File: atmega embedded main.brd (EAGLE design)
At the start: 313.5 x 125.9 mm, 150 parts, among them IC1 ATMEGA328PROUND, K100 SWITCH, K101 SWITCH, K102 SWITCH, K103 SWITCH, K104 SWITCH, K105 SWITCH, K106 SWITCH, K107 SWITCH, K108 SWITCH, K109 SWITCH, K110 SWITCH, K111 SWITCH, K112 SWITCH, K113 SWITCH, K114 SWITCH, K115 SWITCH, K116 SWITCH, K117 SWITCH, K118 SWITCH, K119 SWITCH, K120 SWITCH, K121 SWITCH, K122 SWITCH, K123 SWITCH, K124 SWITCH, K125 SWITCH, K126 SWITCH, K127 SWITCH, K128 SWITCH, K129 SWITCH, K130 SWITCH, K60 SWITCH, K67 SWITCH, K68 SWITCH, K69 SWITCH, K70 SWITCH, K71 SWITCH, K72 SWITCH, K73 SWITCH, K74 SWITCH, K75 SWITCH, K76 SWITCH, K77 SWITCH, K78 SWITCH, K79 SWITCH, K80 SWITCH, K81 SWITCH, K82 SWITCH, K83 SWITCH, K84 SWITCH, K85 SWITCH, K86 SWITCH, K87 SWITCH, K88 SWITCH, K89 SWITCH, K90 SWITCH, K91 SWITCH, K92 SWITCH, K93 SWITCH, K94 SWITCH, K95 SWITCH, K96 SWITCH, K97 SWITCH, K98 SWITCH, K99 SWITCH

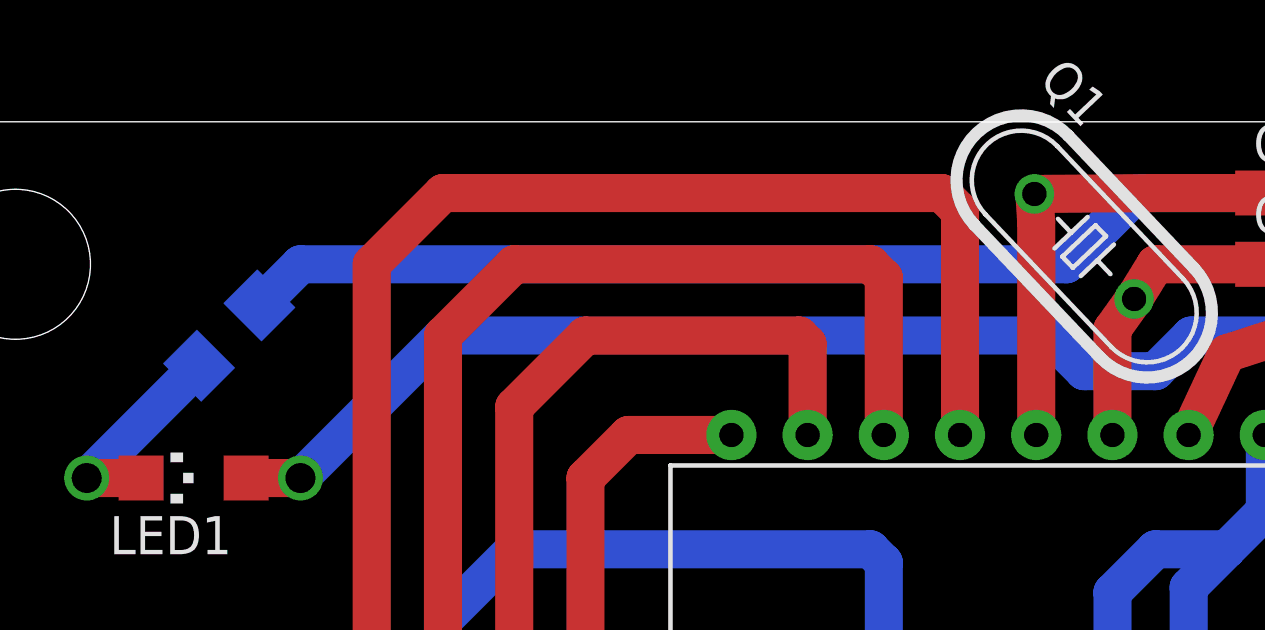
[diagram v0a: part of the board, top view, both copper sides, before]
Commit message: Finished Marko's board and fixed some errors.
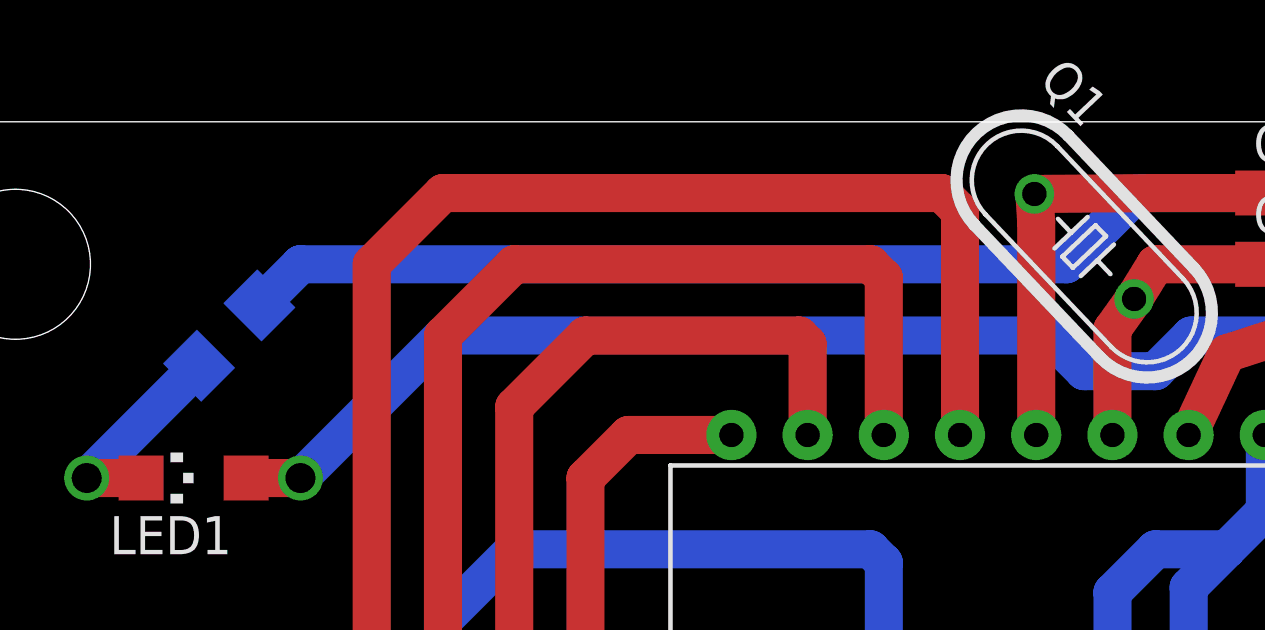
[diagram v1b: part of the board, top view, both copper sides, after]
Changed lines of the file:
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@@
 <wire x1="108.2594" y1="106.875" x2="83.125" y2="106.875" width="1.27" layer="16"/>
 <contactref element="R3" pad="2"/>
-<wire x1="3.380503125" y1="110.255503125" x2="4.75" y2="111.625" width="1.27" layer="16"/>
-<wire x1="4.75" y1="111.625" x2="30.28125" y2="111.625" width="1.27" layer="16"/>
+<wire x1="30.28125" y1="111.625" x2="4.75" y2="111.625" width="1.27" layer="16"/>
 <wire x1="30.28125" y1="111.625" x2="32.65625" y2="114" width="1.27" layer="16"/>
 <wire x1="32.65625" y1="114" x2="80.75" y2="114" width="1.27" layer="16"/>
@@
 <wire x1="120.7875" y1="106.875" x2="120.7875" y2="110.4375" width="1.27" layer="1"/>
 <wire x1="120.7875" y1="110.4375" x2="120.7875" y2="114" width="1.27" layer="1"/>
-<wire x1="3.380503125" y1="110.255503125" x2="3.38050625" y2="110.255503125" width="0" layer="19" extent="16-16"/>
+<wire x1="4.75" y1="111.625" x2="4.75" y2="111.624996875" width="1.27" layer="16"/>
+<wire x1="4.75" y1="111.624996875" x2="3.38050625" y2="110.255503125" width="1.27" layer="16"/>
 </signal>
 <signal name="VCC">
@@
 <via x="-2.375" y="104.5" extent="1-16" drill="1"/>
 <wire x1="-2.375" y1="104.5" x2="1.36949375" y2="108.24449375" width="1.27" layer="16"/>
-<wire x1="1.36949375" y1="108.24449375" x2="1.369496875" y2="108.24449375" width="0" layer="19" extent="16-16"/>
+<wire x1="1.36949375" y1="108.24449375" x2="1.369496875" y2="108.24449375" width="1.27" layer="16"/>
 </signal>
 </signals>

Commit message: Less Horrible for Marko no.1
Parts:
- moved D96 13.1 mm to (117.6, 42.0), turned to 0 degrees
- moved D73 12.8 mm to (117.6, 61.8), turned to 0 degrees
- moved D97 12.7 mm to (117.6, 24.0), turned to 0 degrees
- moved D72 12.5 mm to (117.6, 81.5), turned to 0 degrees
- moved D79 11.6 mm to (-5.25, 63.4), turned to 90 degrees
- moved D45 11.4 mm to (-5.00, 82.4), turned to 90 degrees
- moved D80 11.4 mm to (-5.00, 44.4), turned to 90 degrees
- moved D81 11.4 mm to (-5.00, 25.4), turned to 90 degrees
- moved D82 11.4 mm to (-5.00, 6.44), turned to 90 degrees
- moved LED1 7.21 mm to (5.19, 110.5)
- moved D63 4.72 mm to (22.4, 81.5)
- moved R3 4.61 mm to (1.38, 113.8)
- moved D78 4.26 mm to (22.3, 62.2)
- moved D98 4.26 mm to (164.8, 24.2)
- moved D115 4.01 mm to (288.3, 81.5)
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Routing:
- net ROW5: track 766.2 -> 354.9 mm, vias 2 -> 3
- net ROW3: track 646.0 -> 262.5 mm, vias 2 -> 3
- net ROW4: track 658.2 -> 460.7 mm, vias 2 -> 9
- net COL6: track 277.7 -> 445.6 mm, vias 2 -> 7
- net ROW2: track 600.6 -> 469.0 mm, vias 2 -> 8
- net ROW1: track 382.2 -> 286.5 mm
- net ROW6: track 477.0 -> 557.5 mm, vias 2 -> 9
- net ROW7: track 260.1 -> 333.0 mm, vias 2 -> 4
- net COL1: track 203.5 -> 271.3 mm, vias 1 -> 3
- net COL2: track 316.2 -> 377.5 mm, vias 2 -> 8
- net COL7: track 389.5 -> 448.4 mm, vias 3 -> 5
- net COL3: track 314.8 -> 361.4 mm, vias 2 -> 3
- net COL9: track 431.2 -> 392.3 mm, vias 3 -> 4
- net COL10: track 340.8 -> 364.2 mm, vias 2 -> 1
- net COL5: track 319.6 -> 342.1 mm, vias 1 -> 3
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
